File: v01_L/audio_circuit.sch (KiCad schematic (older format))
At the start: 44 parts, among them P1 CONN_1, P10 CONN_1, P11 CONN_1, P12 CONN_1, P2 CONN_1, P3 CONN_1, P4 CONN_1, P5 CONN_1, P6 CONN_1, P7 CONN_1, P8 CONN_1, P9 CONN_1, U2 TI_TPA6138A2

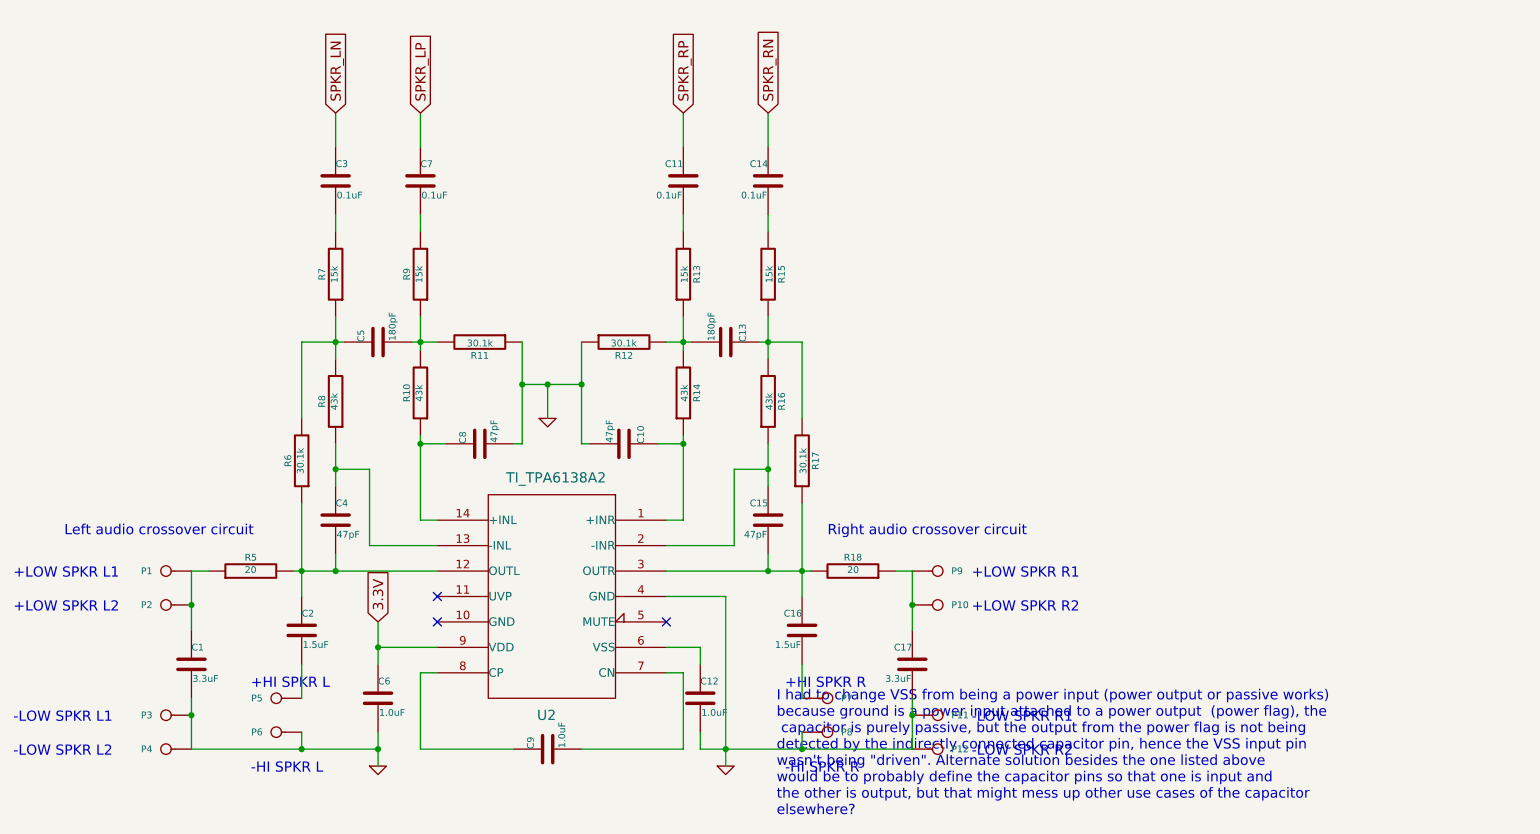
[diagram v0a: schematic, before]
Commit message: Update includes removing right side of audio circuit
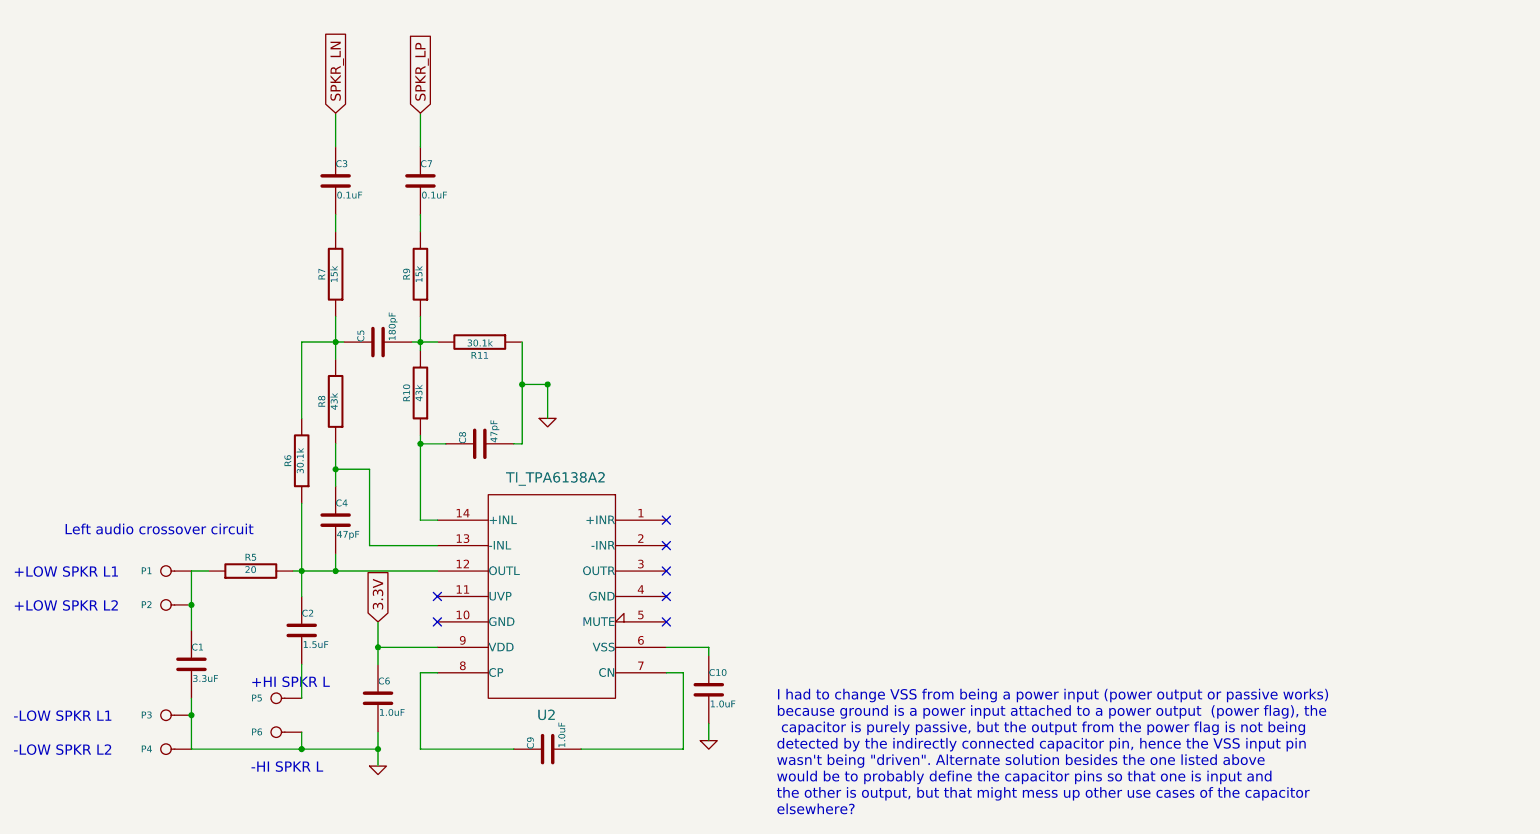
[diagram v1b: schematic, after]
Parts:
- removed C11, C14: 0.1uF, ~, symbol C
- removed C12: 1.0uF, ~, symbol C
- removed C13: 180pF, ~, symbol C
- removed C15: 47pF, ~, symbol C
- removed C16: 1.5uF, ~, symbol C
- removed C17: 3.3uF, ~, symbol C
- removed P10, P11, P12, P7, P8, P9: CONN_1, symbol CONN_1
- removed R12, R17: 30.1k, ~, symbol R
- removed R13, R15: 15k, ~, symbol R
- removed R14, R16: 43k, ~, symbol R
- removed R18: 20, ~, symbol R
- C10: value 47pF -> 1.0uF
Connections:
- net GND: no longer U2.4 (GND)
- net at U2.1 (+INR): no longer C10.1
- net at U2.6 (VSS): now also C10.1
- no-connect marks 3 -> 7
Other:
- note removed: "+HI SPKR R"
- note removed: "+LOW SPKR R1"
- note removed: "+LOW SPKR R2"
- note removed: "-HI SPKR R"
- note removed: "-LOW SPKR R1"
- note removed: "-LOW SPKR R2"
- note removed: "Right audio crossover circuit"
